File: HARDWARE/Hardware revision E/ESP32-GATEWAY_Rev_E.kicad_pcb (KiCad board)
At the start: 2 copper layers, 50.8 x 62.2 mm, 93 parts, among them CON1 NA(NH1x20), Q3 Q12MHz/20pF/30ppm/2P/HC-49SM(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, Q4 BC817-40(SOT23), Q5 BC817-40(SOT23), T1 DTC114YKA, U2 SY8089AAAC(SOT23-5), U3 ESP-WROOM-32, U4 LAN8710A-EZC(QFN32), U5 CH340T(SSOP20W), U9 BAT54C(SOT23-3)

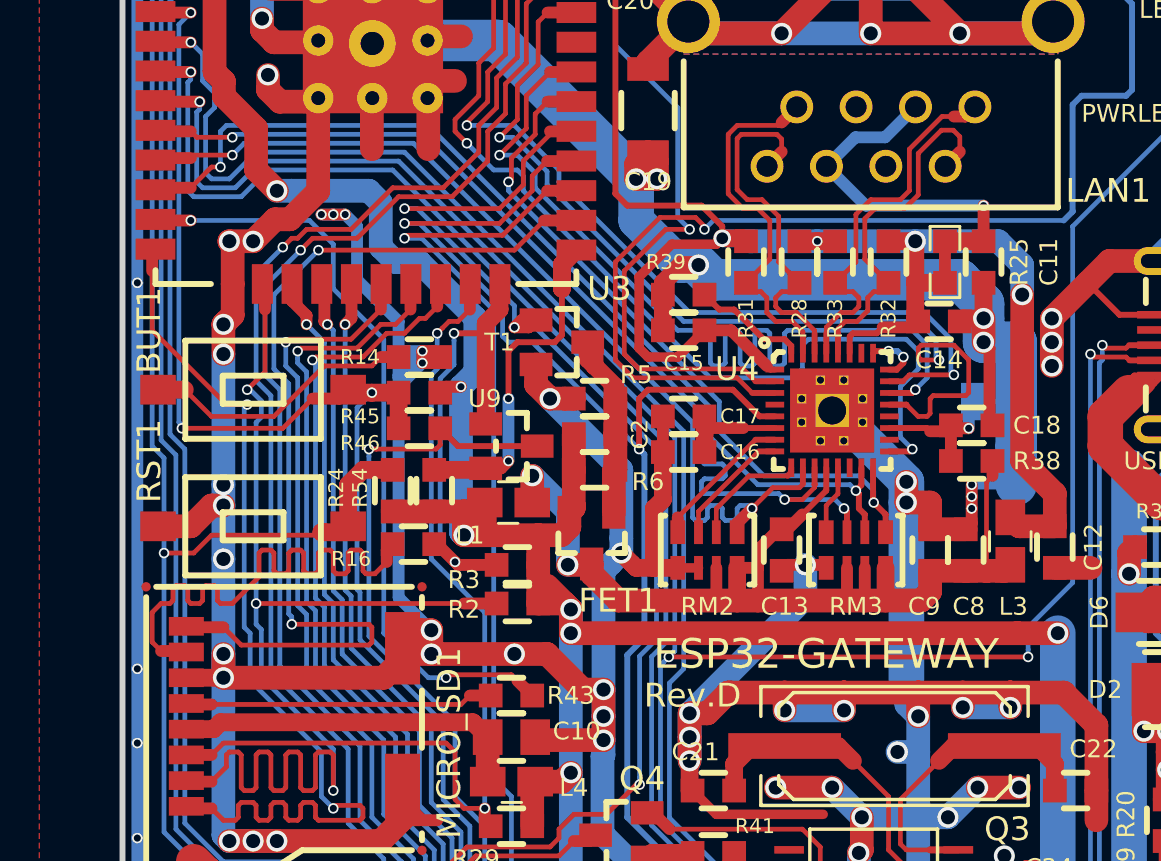
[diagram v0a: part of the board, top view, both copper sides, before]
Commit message: Fix
Wrong sources were uploaded by mistake
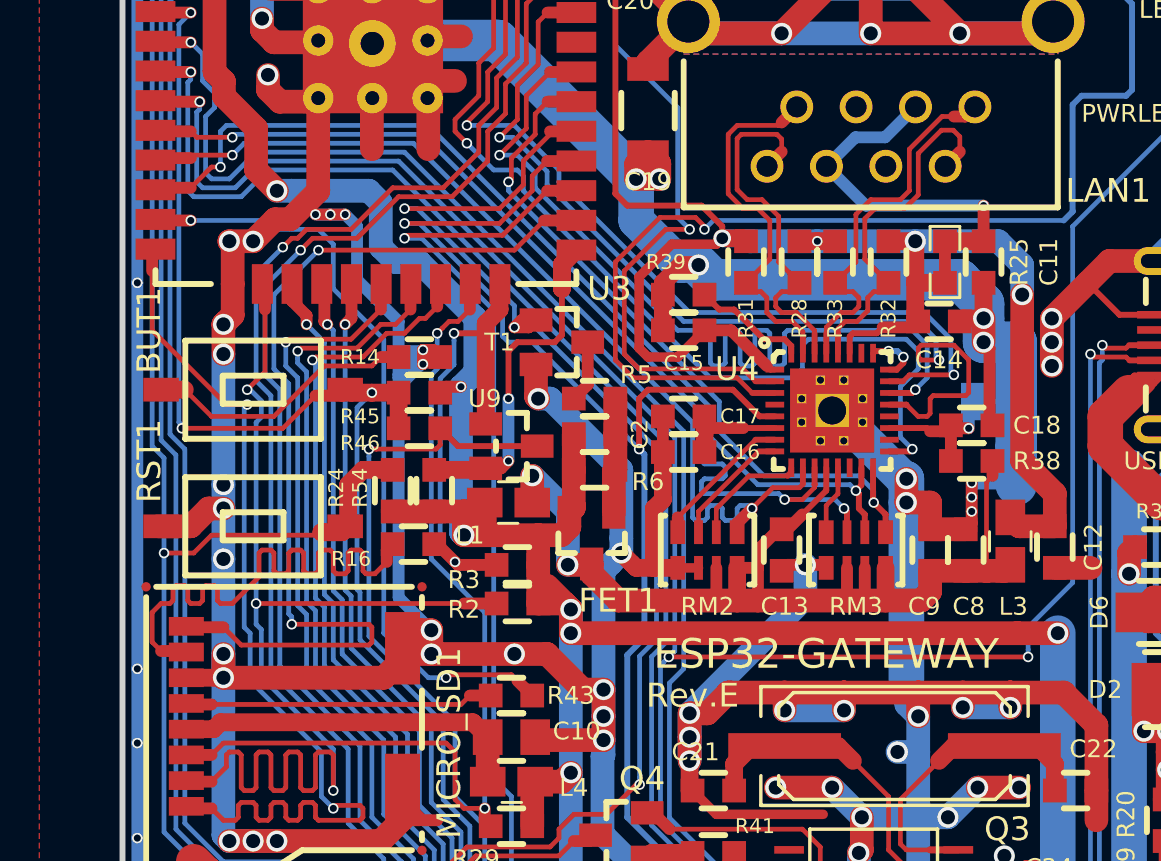
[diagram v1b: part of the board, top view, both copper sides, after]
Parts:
- R5: value NA/R0603 -> 1k/R0603
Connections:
- R5 pad 2: GND -> Net-(R5-Pad2)
- T1 pad 3: Net-(C2-Pad2) -> Net-(R5-Pad2)
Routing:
- net Net-(C2-Pad2): track 8.81 -> 4.89 mm
- net Net-(R5-Pad2): track 0.00 -> 2.66 mm
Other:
- board text added: "Rev.E"
- board text removed: "Rev.D"
